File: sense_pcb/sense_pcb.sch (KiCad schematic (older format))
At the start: 31 parts

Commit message: IC layout done
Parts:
- removed J?: Conn_02x06_Odd_Even, symbol Conn_02x06_Odd_Even
- added J1, J10, J11, J2, J3, J4, J5, J6, J7, J8, J9: TEST_1P, symbol TEST_1P
- C1, C2, C3: renamed from C?; footprint (none) -> Capacitors_SMD:C_1206_HandSoldering
- U14, U23, U5: renamed from U?; footprint (none) -> SMD_Packages:SO-16-N
- gave numbers to parts that had none: 24
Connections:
- net VDD is gone; now on net VCC: U14.16 (VDD), U23.16 (VDD), U5.16 (VDD)
- net VSS is gone; now on net GND: U14.8 (VSS), U23.8 (VSS), U5.8 (VSS)
- net GND: now also J6.1
- net VCC: now also U1.1 (VCC), U10.1 (VCC), U11.1 (VCC), U12.1 (VCC), U13.1 (VCC), U15.1 (VCC), U16.1 (VCC), U17.1 (VCC), U18.1 (VCC), U19.1 (VCC), U2.1 (VCC), U20.1 (VCC), U21.1 (VCC), U22.1 (VCC), U24.1 (VCC), U25.1 (VCC), U26.1 (VCC), U27.1 (VCC), U3.1 (VCC), U4.1 (VCC), U6.1 (VCC), U7.1 (VCC), U8.1 (VCC), U9.1 (VCC), J1.1
- net at U14.10 (B), U23.10 (B), U5.10 (B): now also J10.1
- net at U14.11 (A), U23.11 (A), U5.11 (A): now also J3.1
- net at U5.3 (X): now also J8.1
- net at U5.6 (Inh): now also J2.1
- net at U14.9 (C), U23.9 (C), U5.9 (C): now also J7.1
- net at U14.3 (X): now also J9.1
- net at U14.6 (Inh): now also J4.1
- net at U23.3 (X): now also J11.1
- net at U23.6 (Inh): now also J5.1

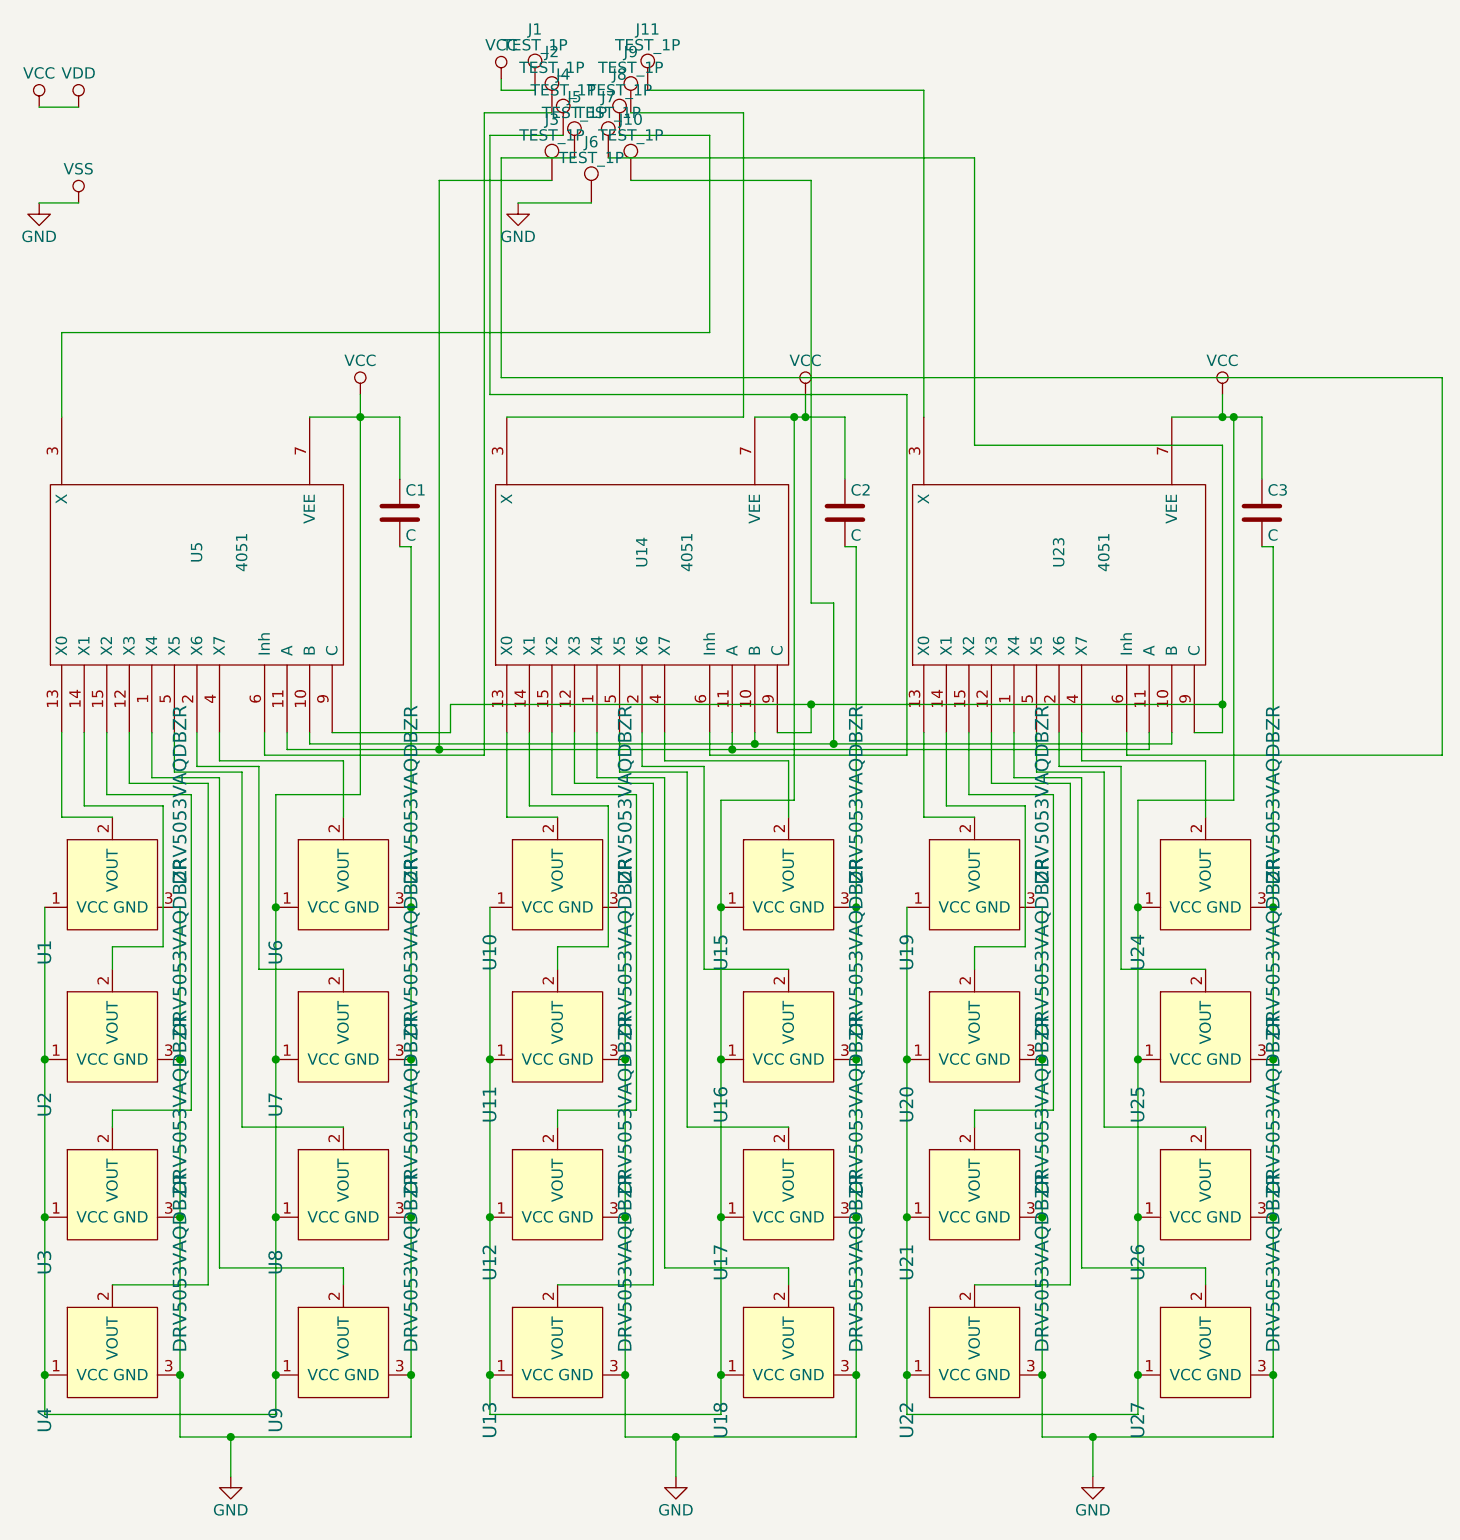
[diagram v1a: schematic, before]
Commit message: removed 2/3 of the sensors from the schematic to shrink it
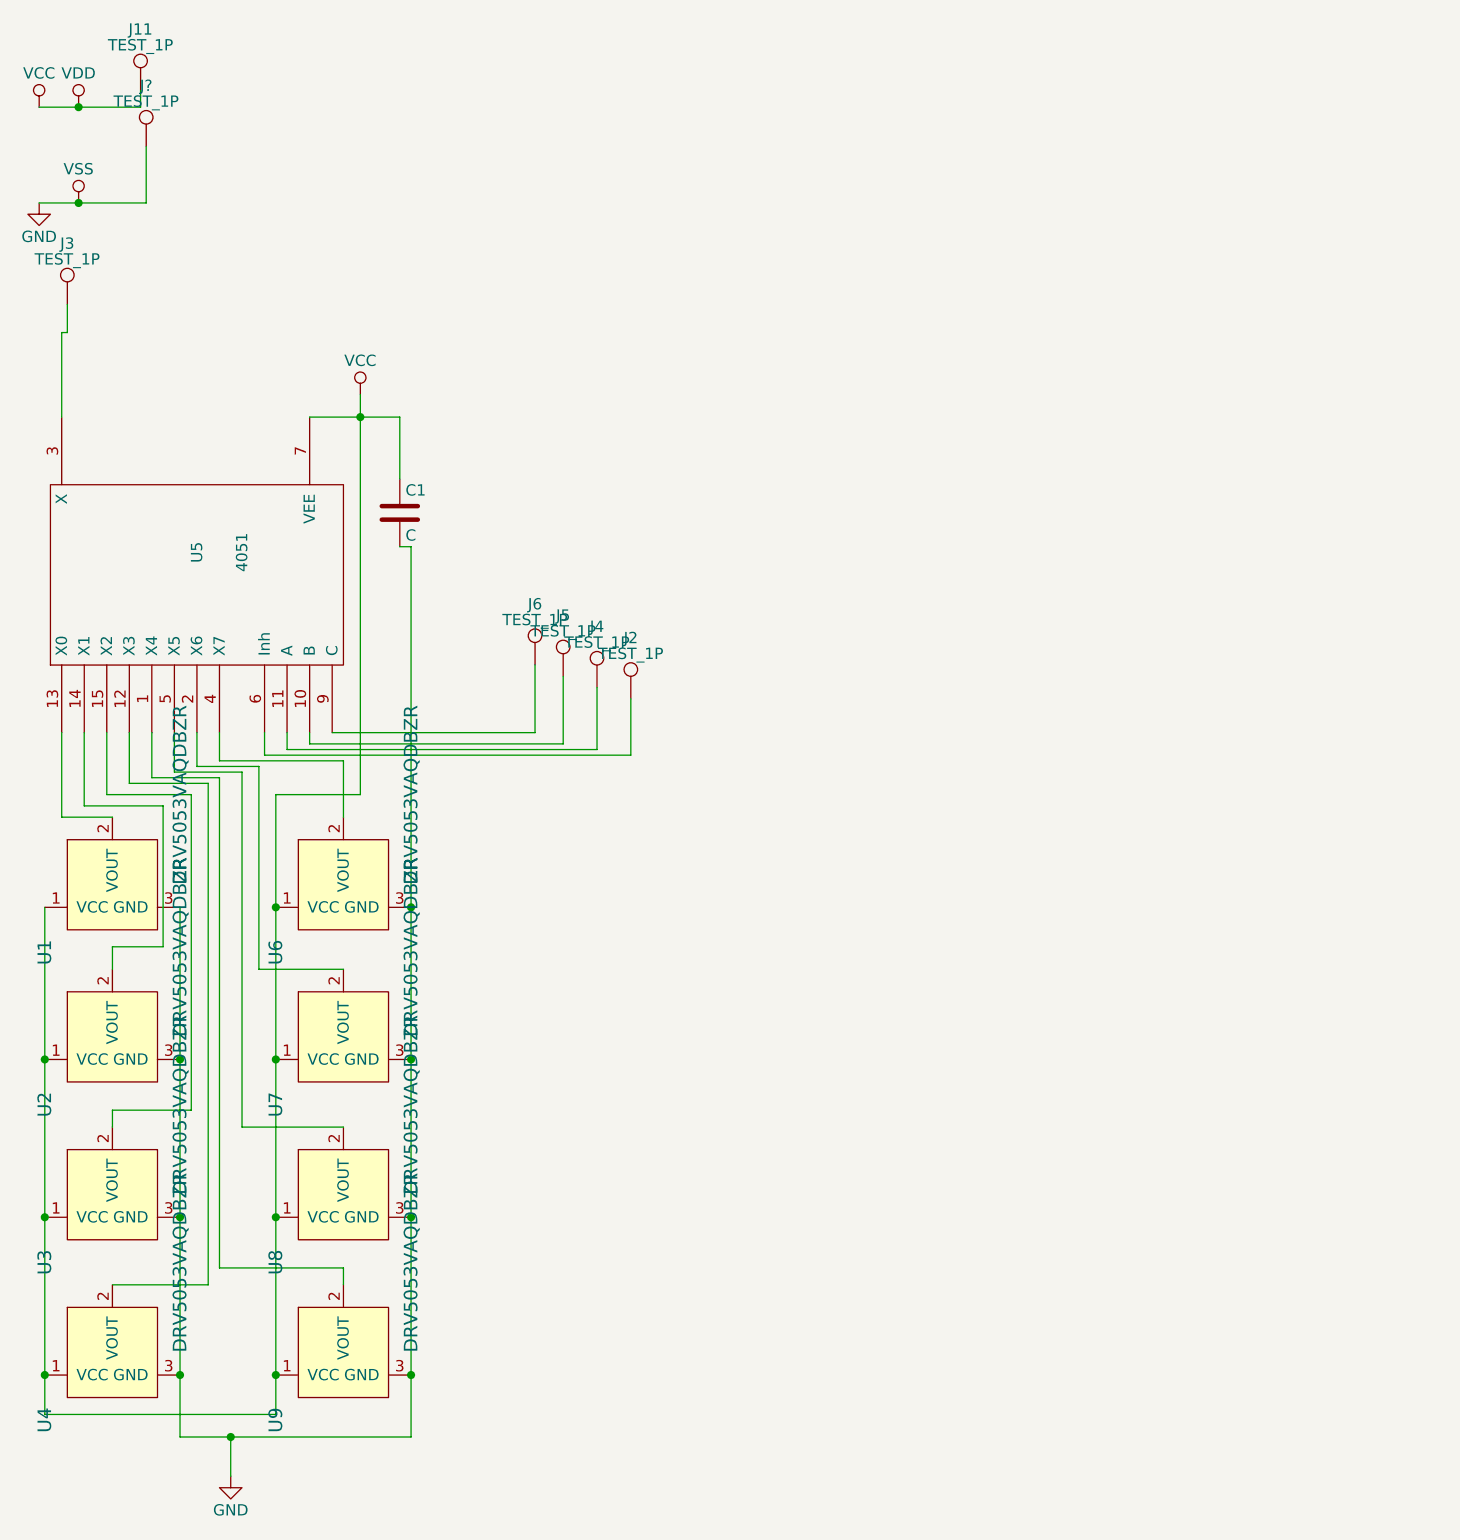
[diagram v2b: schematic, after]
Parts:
- removed C2, C3: C, Capacitors_SMD:C_1206_HandSoldering, symbol C
- removed J1, J10, J7, J8, J9: TEST_1P, symbol TEST_1P
- removed U10, U11, U12, U13, U15, U16, U17, U18, U19, U20, U21, U22, U24, U25, U26, U27: DRV5053VAQDBZR, digikey-footprints:SOT-23-3, symbol DRV5053VAQDBZR
- removed U14, U23: 4051, SMD_Packages:SO-16-N, symbol 4051
- added J?: TEST_1P, symbol TEST_1P
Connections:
- net GND: now also J?.1; no longer J6.1
- net VCC: now also J11.1
- net at U5.10 (B): now also J5.1
- net at U5.11 (A): now also J4.1; no longer J3.1
- net at U5.3 (X): now also J3.1
- net at U5.9 (C): now also J6.1
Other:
- moved on the sheet: J11, J2, J3, J4, J5, J6

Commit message: went over to Kicad 5.0, seems legit so far
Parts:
- C1: symbol C -> sense_pcb-rescue:C
- J1: renamed from J3; footprint (none) -> Measurement_Points:Measurement_Point_Round-SMD-Pad_Small; symbol TEST_1P -> sense_pcb-rescue:TEST_1P
- J2: renamed from J11; footprint (none) -> Measurement_Points:Measurement_Point_Round-SMD-Pad_Small; symbol TEST_1P -> sense_pcb-rescue:TEST_1P
- J3: renamed from J?; footprint (none) -> Measurement_Points:Measurement_Point_Round-SMD-Pad_Small; symbol TEST_1P -> sense_pcb-rescue:TEST_1P
- J4: renamed from J6; footprint (none) -> Measurement_Points:Measurement_Point_Round-SMD-Pad_Small; symbol TEST_1P -> sense_pcb-rescue:TEST_1P
- J5: footprint (none) -> Measurement_Points:Measurement_Point_Round-SMD-Pad_Small; symbol TEST_1P -> sense_pcb-rescue:TEST_1P
- J6: renamed from J4; footprint (none) -> Measurement_Points:Measurement_Point_Round-SMD-Pad_Small; symbol TEST_1P -> sense_pcb-rescue:TEST_1P
- J7: renamed from J2; footprint (none) -> Measurement_Points:Measurement_Point_Round-SMD-Pad_Small; symbol TEST_1P -> sense_pcb-rescue:TEST_1P
- U1, U2, U3, U4, U6, U7, U8, U9: symbol DRV5053VAQDBZR -> dk_Magnetic-Sensors-Linear-Compass-ICs:DRV5053VAQDBZR
- U5: symbol 4051 -> sense_pcb-rescue:4051
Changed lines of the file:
@@
-EESchema Schematic File Version 2
-LIBS:power
-LIBS:device
-LIBS:switches
-LIBS:relays
-LIBS:motors
-LIBS:transistors
-LIBS:conn
-LIBS:linear
-LIBS:regul
-LIBS:74xx
-LIBS:cmos4000
-LIBS:adc-dac
-LIBS:memory
-LIBS:xilinx
-LIBS:microcontrollers
-LIBS:dsp
-LIBS:microchip
-LIBS:analog_switches
-LIBS:motorola
-LIBS:texas
-LIBS:intel
-LIBS:audio
-LIBS:interface
-LIBS:digital-audio
-LIBS:philips
-LIBS:display
-LIBS:cypress
-LIBS:siliconi
-LIBS:opto
-LIBS:atmel
-LIBS:contrib
-LIBS:valves
+EESchema Schematic File Version 4
 LIBS:sense_pcb-cache
-EELAYER 25 0
+EELAYER 26 0
 EELAYER END
 $Descr A4 11693 8268
@@
 $EndDescr
 $Comp
-L 4051 U5
+L sense_pcb-rescue:4051 U5
 U 1 1 5C79D3AB
 P 1675 2900
@@
 $EndComp
 $Comp
-L DRV5053VAQDBZR U1
+L dk_Magnetic-Sensors-Linear-Compass-ICs:DRV5053VAQDBZR U1
 U 1 1 5C79D70C
 P 1300 4475
@@
 $EndComp
 $Comp
-L DRV5053VAQDBZR U2
+L dk_Magnetic-Sensors-Linear-Compass-ICs:DRV5053VAQDBZR U2
 U 1 1 5C79DA4D
 P 1300 5150
@@
 $EndComp
 $Comp
-L DRV5053VAQDBZR U3
+L dk_Magnetic-Sensors-Linear-Compass-ICs:DRV5053VAQDBZR U3
 U 1 1 5C79DB6B
 P 1300 5850
@@
 $EndComp
 $Comp
-L DRV5053VAQDBZR U4
+L dk_Magnetic-Sensors-Linear-Compass-ICs:DRV5053VAQDBZR U4
 U 1 1 5C79DC91
 P 1300 6550
@@
 $EndComp
 $Comp
-L C C1
+L sense_pcb-rescue:C C1
 U 1 1 5C79F1DF
 P 2575 2625
@@
 $EndComp
 $Comp
-L DRV5053VAQDBZR U6
+L dk_Magnetic-Sensors-Linear-Compass-ICs:DRV5053VAQDBZR U6
 U 1 1 5C79F8D1
 P 2325 4475
@@
 $EndComp
 $Comp
-L DRV5053VAQDBZR U7
+L dk_Magnetic-Sensors-Linear-Compass-ICs:DRV5053VAQDBZR U7
 U 1 1 5C79F8E0
 P 2325 5150
@@
 $EndComp
 $Comp
-L DRV5053VAQDBZR U8
+L dk_Magnetic-Sensors-Linear-Compass-ICs:DRV5053VAQDBZR U8
 U 1 1 5C79F8EF
 P 2325 5850
@@
 $EndComp
 $Comp
-L DRV5053VAQDBZR U9
+L dk_Magnetic-Sensors-Linear-Compass-ICs:DRV5053VAQDBZR U9
 U 1 1 5C79F8FE
 P 2325 6550
@@
 $EndComp
 Wire Wire Line
-	1000 4375 1000 6625
+	1000 4375 1000 5050
 Connection ~ 1000 5050
 Connection ~ 1000 5750
@@
 	1000 6625 2025 6625
 Wire Wire Line
-	2025 6625 2025 3875
+	2025 6625 2025 6450
 Connection ~ 1000 6450
 Connection ~ 2025 6450
@@
 Connection ~ 2025 5050
 Wire Wire Line
-	2625 2775 2625 6725
+	2625 2775 2625 4375
 Connection ~ 2625 5050
 Connection ~ 2625 5750
 Wire Wire Line
-	1600 4375 1600 6725
-Wire Wire Line
-	1600 6725 2625 6725
+	1600 4375 1600 5050
+Wire Wire Line
+	1600 6725 1825 6725
 Connection ~ 2625 6450
 Connection ~ 1600 6450
@@
 	2575 2475 2575 2200
 Wire Wire Line
-	2575 2200 2175 2200
-$Comp
-L GND #PWR5
+	2575 2200 2400 2200
+$Comp
+L power:GND #PWR05
 U 1 1 5C79FE8A
 P 1825 6900
-F 0 "#PWR5" H 1825 6650 50  0001 C CNN
+F 0 "#PWR05" H 1825 6650 50  0001 C CNN
 F 1 "GND" H 1825 6750 50  0000 C CNN
 F 2 "" H 1825 6900 50  0001 C CNN
@@
 $EndComp
 $Comp
-L VCC #PWR6
+L power:VCC #PWR06
 U 1 1 5C79FEB2
 P 2400 2100
-F 0 "#PWR6" H 2400 1950 50  0001 C CNN
+F 0 "#PWR06" H 2400 1950 50  0001 C CNN
 F 1 "VCC" H 2400 2250 50  0000 C CNN
 F 2 "" H 2400 2100 50  0001 C CNN
@@
 $EndComp
 Wire Wire Line
-	2400 2100 2400 3875
+	2400 2100 2400 2200
 Connection ~ 2400 2200
 Wire Wire Line
@@
 Connection ~ 2025 4375
 $Comp
-L VCC #PWR1
+L power:VCC #PWR01
 U 1 1 5C7A43BC
 P 975 825
-F 0 "#PWR1" H 975 675 50  0001 C CNN
+F 0 "#PWR01" H 975 675 50  0001 C CNN
 F 1 "VCC" H 975 975 50  0000 C CNN
 F 2 "" H 975 825 50  0001 C CNN
@@
 $EndComp
 $Comp
-L GND #PWR2
+L power:GND #PWR02
 U 1 1 5C7A440E
 P 975 1250
-F 0 "#PWR2" H 975 1000 50  0001 C CNN
+F 0 "#PWR02" H 975 1000 50  0001 C CNN
 F 1 "GND" H 975 1100 50  0000 C CNN
 F 2 "" H 975 1250 50  0001 C CNN
@@
 $EndComp
 $Comp
-L VDD #PWR3
+L power:VDD #PWR03
 U 1 1 5C7A4460
 P 1150 825
-F 0 "#PWR3" H 1150 675 50  0001 C CNN
+F 0 "#PWR03" H 1150 675 50  0001 C CNN
 F 1 "VDD" H 1150 975 50  0000 C CNN
 F 2 "" H 1150 825 50  0001 C CNN
@@
 $EndComp
 $Comp
-L VSS #PWR4
+L power:VSS #PWR04
 U 1 1 5C7A44B2
 P 1150 1250
-F 0 "#PWR4" H 1150 1100 50  0001 C CNN
+F 0 "#PWR04" H 1150 1100 50  0001 C CNN
 F 1 "VSS" H 1150 1400 50  0000 C CNN
 F 2 "" H 1150 1250 50  0001 C CNN
@@
 $EndComp
 Wire Wire Line
-	975  1250 1450 1250
-Wire Wire Line
-	975  825  1425 825
-$Comp
-L TEST_1P J11
+	975  1250 1150 1250
+Wire Wire Line
+	975  825  1150 825
+$Comp
+L sense_pcb-rescue:TEST_1P J2
 U 1 1 5C7A62DE
 P 1425 750
-F 0 "J11" H 1425 1020 50  0000 C CNN
+F 0 "J2" H 1425 1020 50  0000 C CNN
 F 1 "TEST_1P" H 1425 950 50  0000 C CNN
-F 2 "" H 1625 750 50  0001 C CNN
+F 2 "Measurement_Points:Measurement_Point_Round-SMD-Pad_Small" H 1625 750 50  0001 C CNN
 F 3 "" H 1625 750 50  0001 C CNN
 	1    1425 750
@@
 $EndComp
 $Comp
-L TEST_1P J2
+L sense_pcb-rescue:TEST_1P J7
 U 1 1 5C7A634B
 P 3600 3450
-F 0 "J2" H 3600 3720 50  0000 C CNN
+F 0 "J7" H 3600 3720 50  0000 C CNN
 F 1 "TEST_1P" H 3600 3650 50  0000 C CNN
-F 2 "" H 3800 3450 50  0001 C CNN
+F 2 "Measurement_Points:Measurement_Point_Round-SMD-Pad_Small" H 3800 3450 50  0001 C CNN
 F 3 "" H 3800 3450 50  0001 C CNN
 	1    3600 3450
@@
 $EndComp
 $Comp
-L TEST_1P J4
+L sense_pcb-rescue:TEST_1P J6
 U 1 1 5C7A64AA
 P 3450 3400
-F 0 "J4" H 3450 3670 50  0000 C CNN
+F 0 "J6" H 3450 3670 50  0000 C CNN
 F 1 "TEST_1P" H 3450 3600 50  0000 C CNN
-F 2 "" H 3650 3400 50  0001 C CNN
+F 2 "Measurement_Points:Measurement_Point_Round-SMD-Pad_Small" H 3650 3400 50  0001 C CNN
 F 3 "" H 3650 3400 50  0001 C CNN
 	1    3450 3400
@@
 $EndComp
 $Comp
-L TEST_1P J5
+L sense_pcb-rescue:TEST_1P J5
 U 1 1 5C7A6507
 P 3300 3350
 F 0 "J5" H 3300 3620 50  0000 C CNN
 F 1 "TEST_1P" H 3300 3550 50  0000 C CNN
-F 2 "" H 3500 3350 50  0001 C CNN
+F 2 "Measurement_Points:Measurement_Point_Round-SMD-Pad_Small" H 3500 3350 50  0001 C CNN
 F 3 "" H 3500 3350 50  0001 C CNN
 	1    3300 3350
@@
 $EndComp
 $Comp
-L TEST_1P J3
+L sense_pcb-rescue:TEST_1P J1
 U 1 1 5C7A6642
 P 1100 1700
-F 0 "J3" H 1100 1970 50  0000 C CNN
+F 0 "J1" H 1100 1970 50  0000 C CNN
 F 1 "TEST_1P" H 1100 1900 50  0000 C CNN
-F 2 "" H 1300 1700 50  0001 C CNN
+F 2 "Measurement_Points:Measurement_Point_Round-SMD-Pad_Small" H 1300 1700 50  0001 C CNN
 F 3 "" H 1300 1700 50  0001 C CNN
 	1    1100 1700
@@
 $EndComp
 $Comp
-L TEST_1P J6
+L sense_pcb-rescue:TEST_1P J4
 U 1 1 5C7A66CF
 P 3175 3300
-F 0 "J6" H 3175 3570 50  0000 C CNN
+F 0 "J4" H 3175 3570 50  0000 C CNN
 F 1 "TEST_1P" H 3175 3500 50  0000 C CNN
-F 2 "" H 3375 3300 50  0001 C CNN
+F 2 "Measurement_Points:Measurement_Point_Round-SMD-Pad_Small" H 3375 3300 50  0001 C CNN
 F 3 "" H 3375 3300 50  0001 C CNN
 	1    3175 3300
@@
 $EndComp
 $Comp
-L TEST_1P J?
+L sense_pcb-rescue:TEST_1P J3
 U 1 1 5C875137
 P 1450 1000
-F 0 "J?" H 1450 1270 50  0000 C CNN
+F 0 "J3" H 1450 1270 50  0000 C CNN
 F 1 "TEST_1P" H 1450 1200 50  0000 C CNN
-F 2 "" H 1650 1000 50  0001 C CNN
+F 2 "Measurement_Points:Measurement_Point_Round-SMD-Pad_Small" H 1650 1000 50  0001 C CNN
 F 3 "" H 1650 1000 50  0001 C CNN
 	1    1450 1000
@@
 Wire Wire Line
 	3600 3700 3600 3450
+Wire Wire Line
+	1000 5050 1000 5750
+Wire Wire Line
+	1000 5750 1000 6450
+Wire Wire Line
+	1000 6450 1000 6625
+Wire Wire Line
+	2025 6450 2025 5750
+Wire Wire Line
+	2025 5750 2025 5050
+Wire Wire Line
+	2025 5050 2025 4375
+Wire Wire Line
+	2625 5050 2625 5750
+Wire Wire Line
+	2625 5750 2625 6450
+Wire Wire Line
+	2625 6450 2625 6725
+Wire Wire Line
+	1600 6450 1600 6725
+Wire Wire Line
+	1600 5750 1600 6450
+Wire Wire Line
+	1600 5050 1600 5750
+Wire Wire Line
+	2625 4375 2625 5050
+Wire Wire Line
+	2400 2200 2175 2200
+Wire Wire Line
+	2400 2200 2400 3875
+Wire Wire Line
+	1825 6725 2625 6725
+Wire Wire Line
+	2025 4375 2025 3875
+Wire Wire Line
+	1150 1250 1450 1250
+Wire Wire Line
+	1150 825  1425 825
 $EndSCHEMATC
